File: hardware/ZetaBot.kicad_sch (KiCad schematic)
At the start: 16 parts, among them J1 USB C PD Modulle, J2 Conn_01x05, J3 MOTOR_L, J4 MOTOR_R, SW1 SW_SPDT, U1 RPI5, U2 Buck Converter

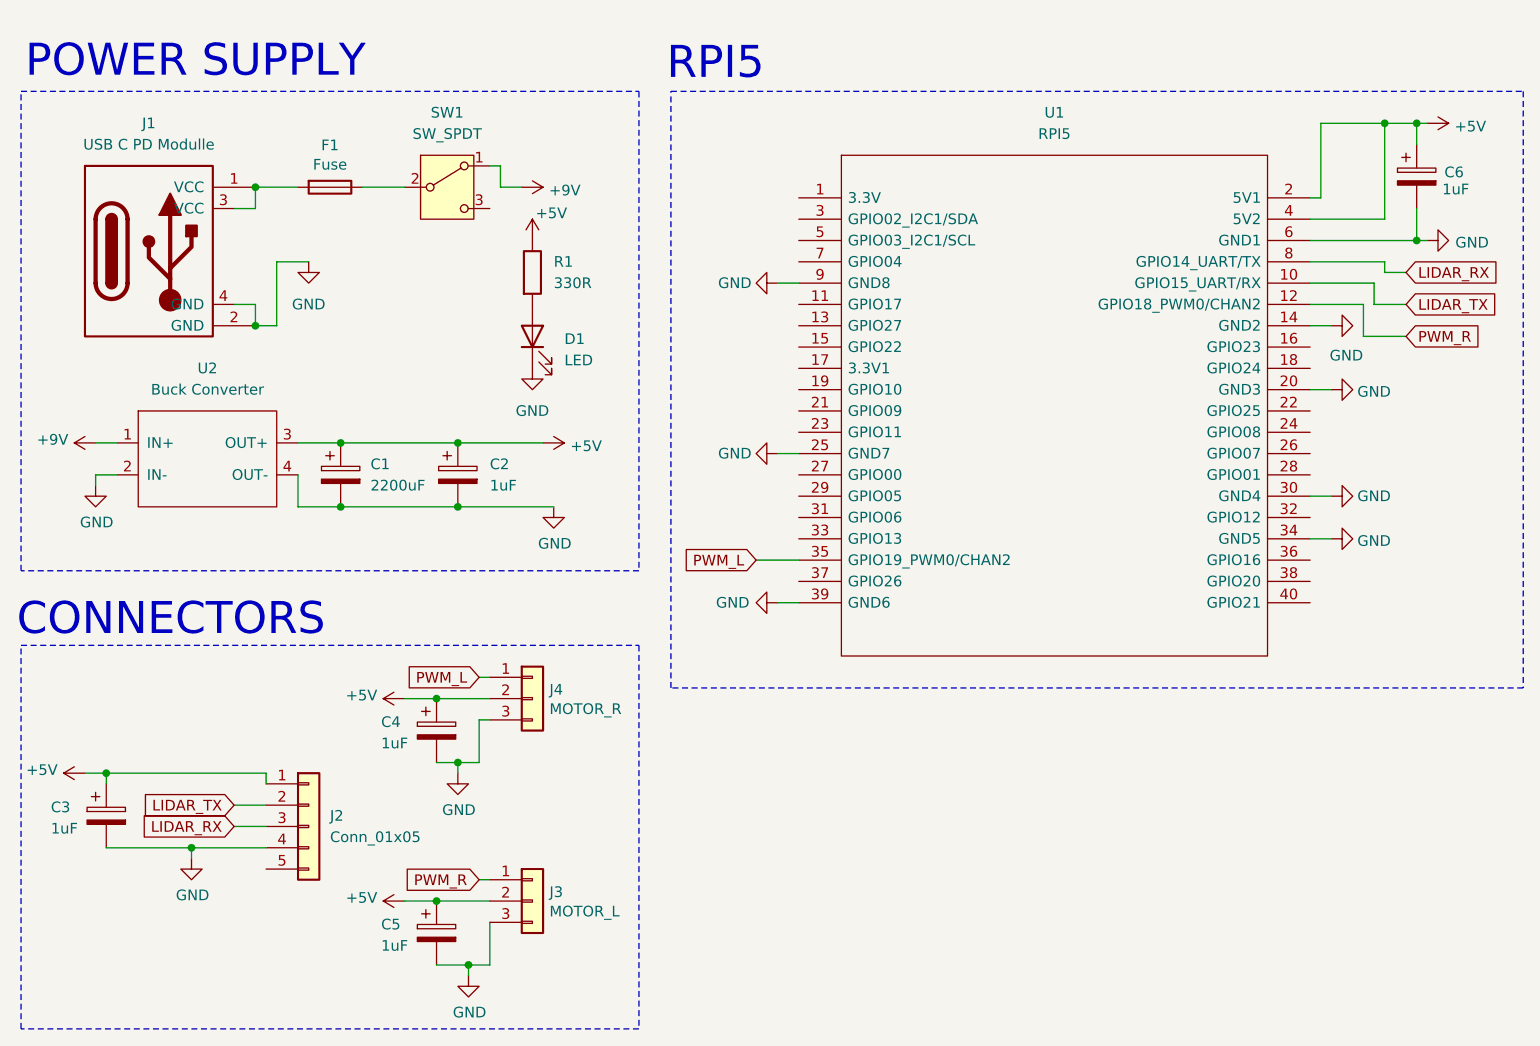
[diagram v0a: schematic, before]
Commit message: Added header for Gyro and moved switch to post buck converter.
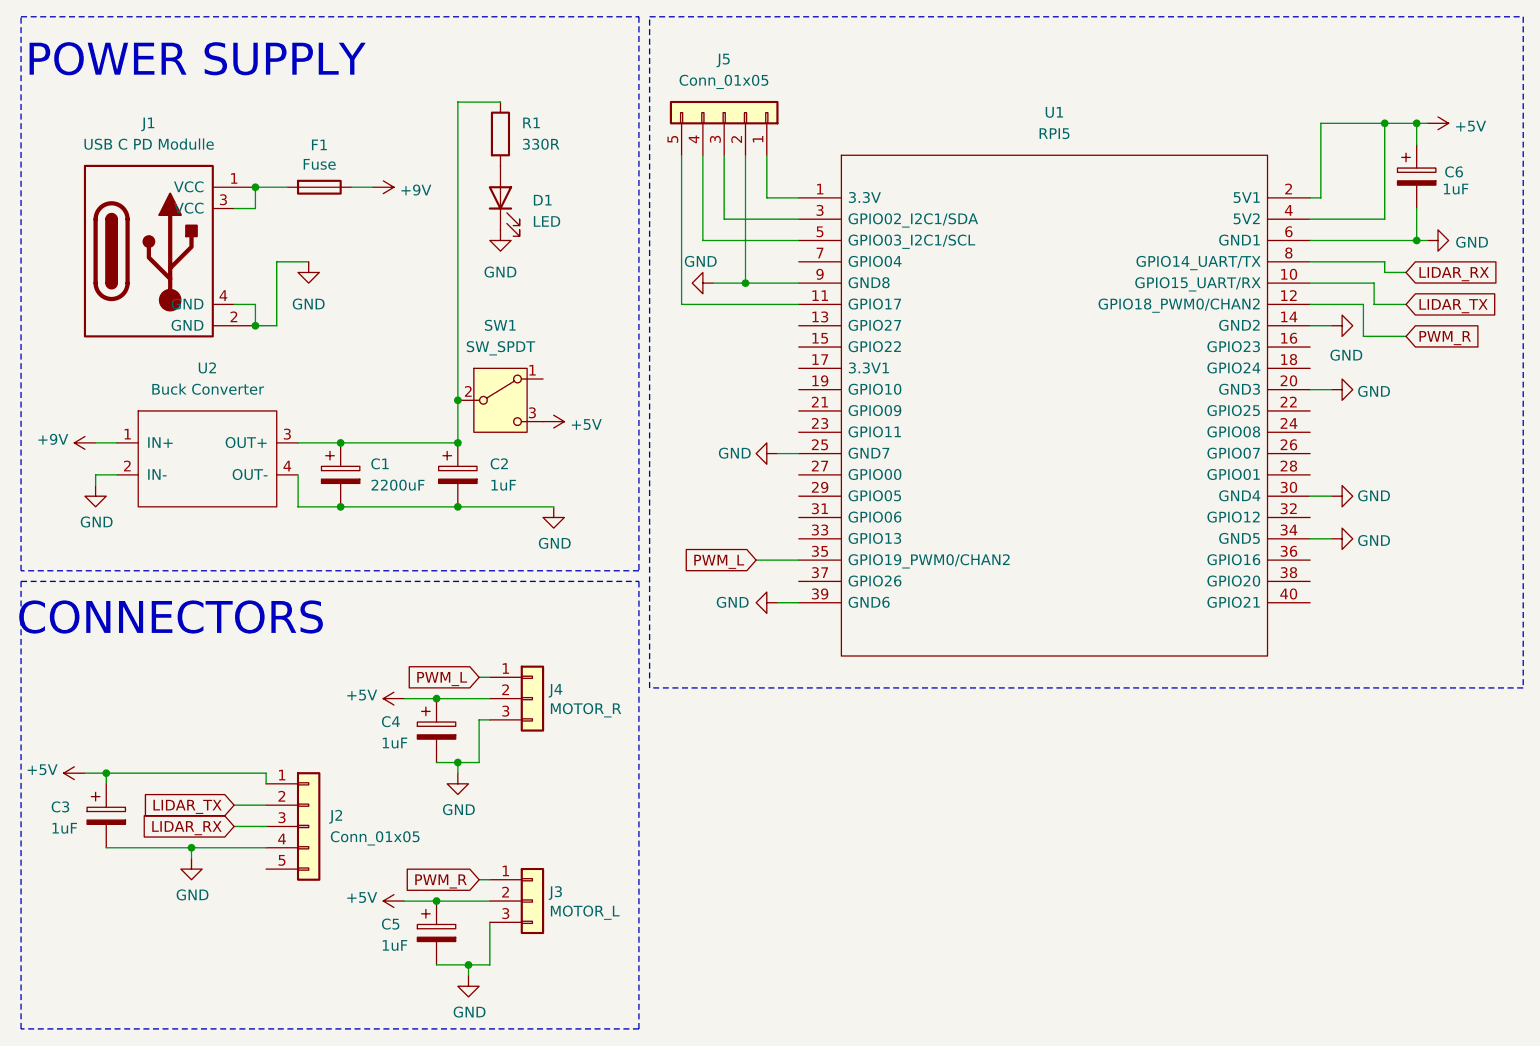
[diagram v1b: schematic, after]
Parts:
- added J5: Conn_01x05, Connector_PinHeader_2.54mm:PinHeader_1x05_P2.54mm_Vertical, symbol Connector_Generic:Conn_01x05
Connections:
- net +5V: now also SW1.3 (C); no longer C1.1, C2.1, R1.1, U2.3 (OUT+)
- net +9V: now also F1.1; no longer SW1.1 (A)
- net GND: now also J5.2 (Pin_2)
- net at SW1.2 (B): now also C1.1, C2.1, R1.1, U2.3 (OUT+); no longer F1.1
- net at U1.1 (3.3V): now also J5.1 (Pin_1)
- net at U1.11 (GPIO17): now also J5.5 (Pin_5)
- net at U1.3 (GPIO02_I2C1/SDA): now also J5.3 (Pin_3)
- net at U1.5 (GPIO03_I2C1/SCL): now also J5.4 (Pin_4)
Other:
- note removed: "RPI5"
- moved on the sheet: D1, F1, R1, SW1
